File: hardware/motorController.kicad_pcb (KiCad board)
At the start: 2 copper layers, 48.8 x 38 mm, 31 parts, among them J1 CONN_14X1, M1 Mounting Hole, M2 Mounting Hole, M3 Mounting Hole, M4 Mounting Hole, P1 CONN_1, P2 CONN_1, P3 CONN_1, P4 CONN_1, Q1 MOSFET-N, U1 7408, U2 MC33926

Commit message: v1 motor controller
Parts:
- moved C2 0.40 mm to (149.6, 120.1)
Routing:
- net GND: track 15.9 -> 41.8 mm

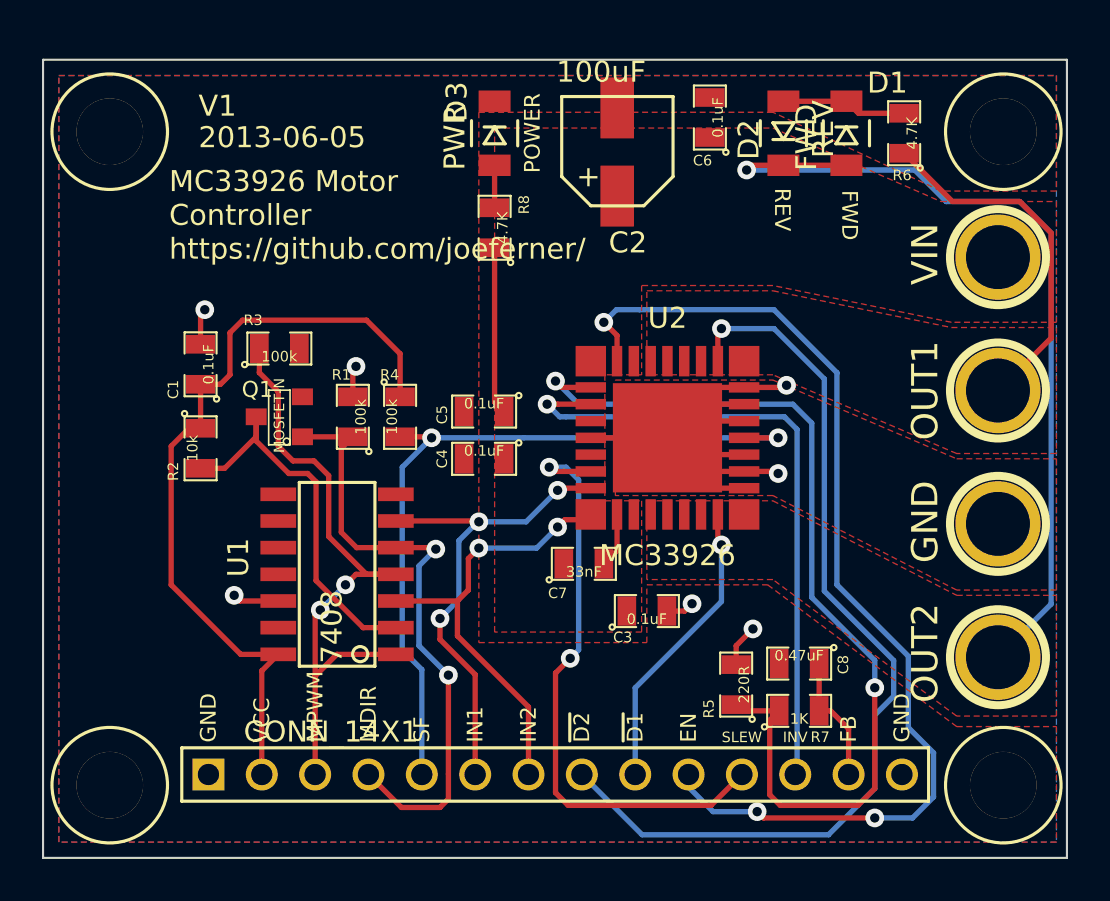
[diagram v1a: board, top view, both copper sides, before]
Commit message: fixed pin numbering on motor controller
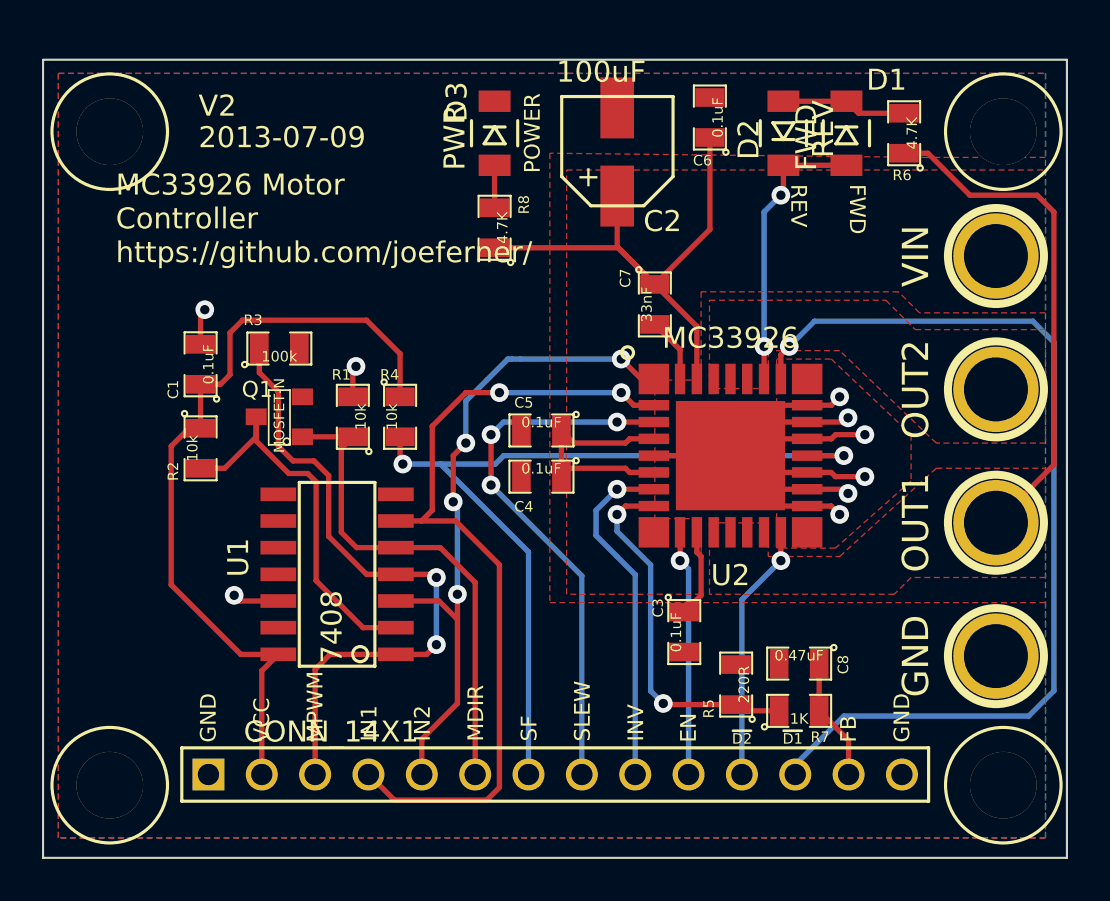
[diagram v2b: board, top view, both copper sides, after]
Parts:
- R1, R4: value 100k -> 10k
- moved C7 12.8 mm to (151.4, 127.4), turned to 270 degrees
- moved P3 12.8 mm to (167.6, 131.4)
- moved P2 6.30 mm to (167.6, 137.8)
- moved P4 6.30 mm to (167.6, 144.1)
- moved U2 3.12 mm to (155.0, 134.6), turned to 0 degrees
- moved C5 2.87 mm to (146.0, 133.4)
- moved C4 2.86 mm to (146.0, 135.6)
- moved C3 2.04 mm to (152.8, 143.0), turned to 270 degrees
- moved P1 0.11 mm to (167.6, 125.1)
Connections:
- J1 pad 11: /SLEW -> /D2#
- J1 pad 12: /INV -> /D1#
- J1 pad 4: /MDIR -> /IN1
- J1 pad 5: /SF -> /IN2
- J1 pad 6: /IN1 -> /MDIR
- J1 pad 7: /IN2 -> /SF
- J1 pad 8: /D2# -> /SLEW
- J1 pad 9: /D1# -> /INV
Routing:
- net /EN: track 49.8 -> 11.7 mm, vias 3 -> 1
- net VDD: track 7.98 -> 42.5 mm
- net /D2#: track 44.5 -> 12.3 mm
- net /D1#: track 13.9 -> 46.1 mm
- net /OUT2: track 41.8 -> 13.6 mm, vias 1 -> 2
- net N-0000010: track 45.1 -> 17.5 mm
- net /IN1: track 23.2 -> 39.6 mm, vias 3 -> 2
- net /INV: track 30.7 -> 16.5 mm
- net /IN2: track 21.2 -> 32.3 mm, vias 2 -> 4
- net /OUT1: track 17.1 -> 24.2 mm
- net GND: track 41.8 -> 48.1 mm, vias 7 -> 9
- net /MDIR: track 29.4 -> 23.7 mm, vias 2 -> 0
- net /SF: track 36.4 -> 40.8 mm
- net /SLEW: track 28.5 -> 26.0 mm, vias 2 -> 3
- net N-0000018: track 2.36 -> 3.09 mm
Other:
- board text added: "2013-07-09"
- board text added: "V2"
- board text removed: "2013-06-05"
- board text removed: "V1"

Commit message: add pullups to motorcontroller
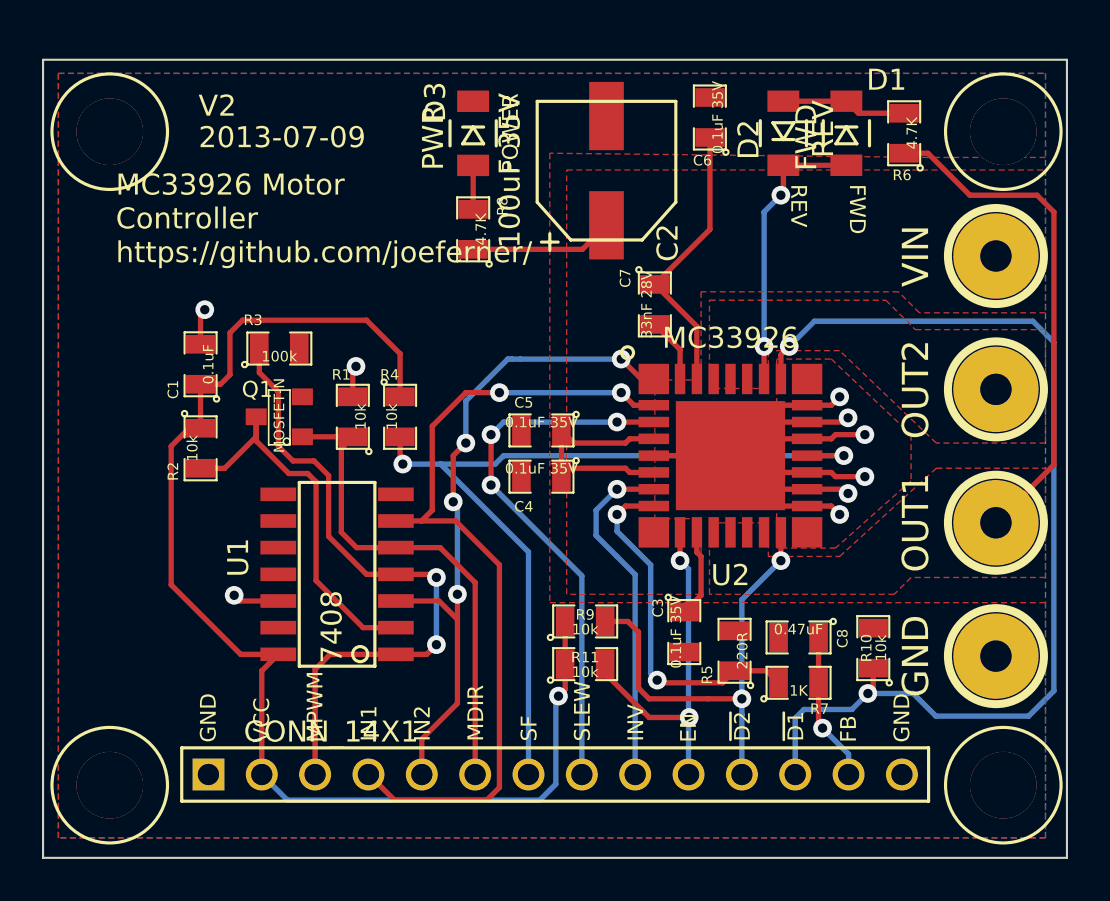
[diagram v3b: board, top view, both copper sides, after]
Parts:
- added R10: 10k, SM0805, F.Cu at (161.8, 143.8)
- added R11: 10k, SM0805, F.Cu at (148.1, 144.5)
- added R9: 10k, SM0805, F.Cu at (148.1, 142.5)
- C2: value 100uF -> 100uF 35V; footprint CAP-CAN-5mm -> CAP-CAN-6.30mm
- C3, C4, C5, C6: value 0.1uF -> 0.1uF 35V
- C7: value 33nF -> 33nF 28V
- moved R5 1.61 mm to (155.2, 143.9)
- moved R7 1.34 mm to (158.2, 145.4)
- moved C8 1.24 mm to (158.2, 143.3)
- moved R8 1.02 mm to (142.7, 123.8)
- moved C2 1.02 mm to (149.1, 121.0), turned to 90 degrees
- moved D3 1.02 mm to (142.7, 119.3)
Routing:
- net VCC: track 37.6 -> 60.4 mm, vias 0 -> 1
- net /D2#: track 12.3 -> 21.9 mm, vias 1 -> 2
- net VDD: track 42.5 -> 36.0 mm
- net /EN: track 11.7 -> 17.3 mm, vias 1 -> 2
- net /D1#: track 46.1 -> 50.0 mm, vias 1 -> 2
- net /FB: track 5.86 -> 7.12 mm, vias 0 -> 1
- net N-000008: track 17.5 -> 16.9 mm
